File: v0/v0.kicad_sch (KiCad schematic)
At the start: 20 parts, among them CON1 SNES-CONN, U1 SN74LV165APWR, U2 SN74LV165APWR, U3 SN74LV165APWR

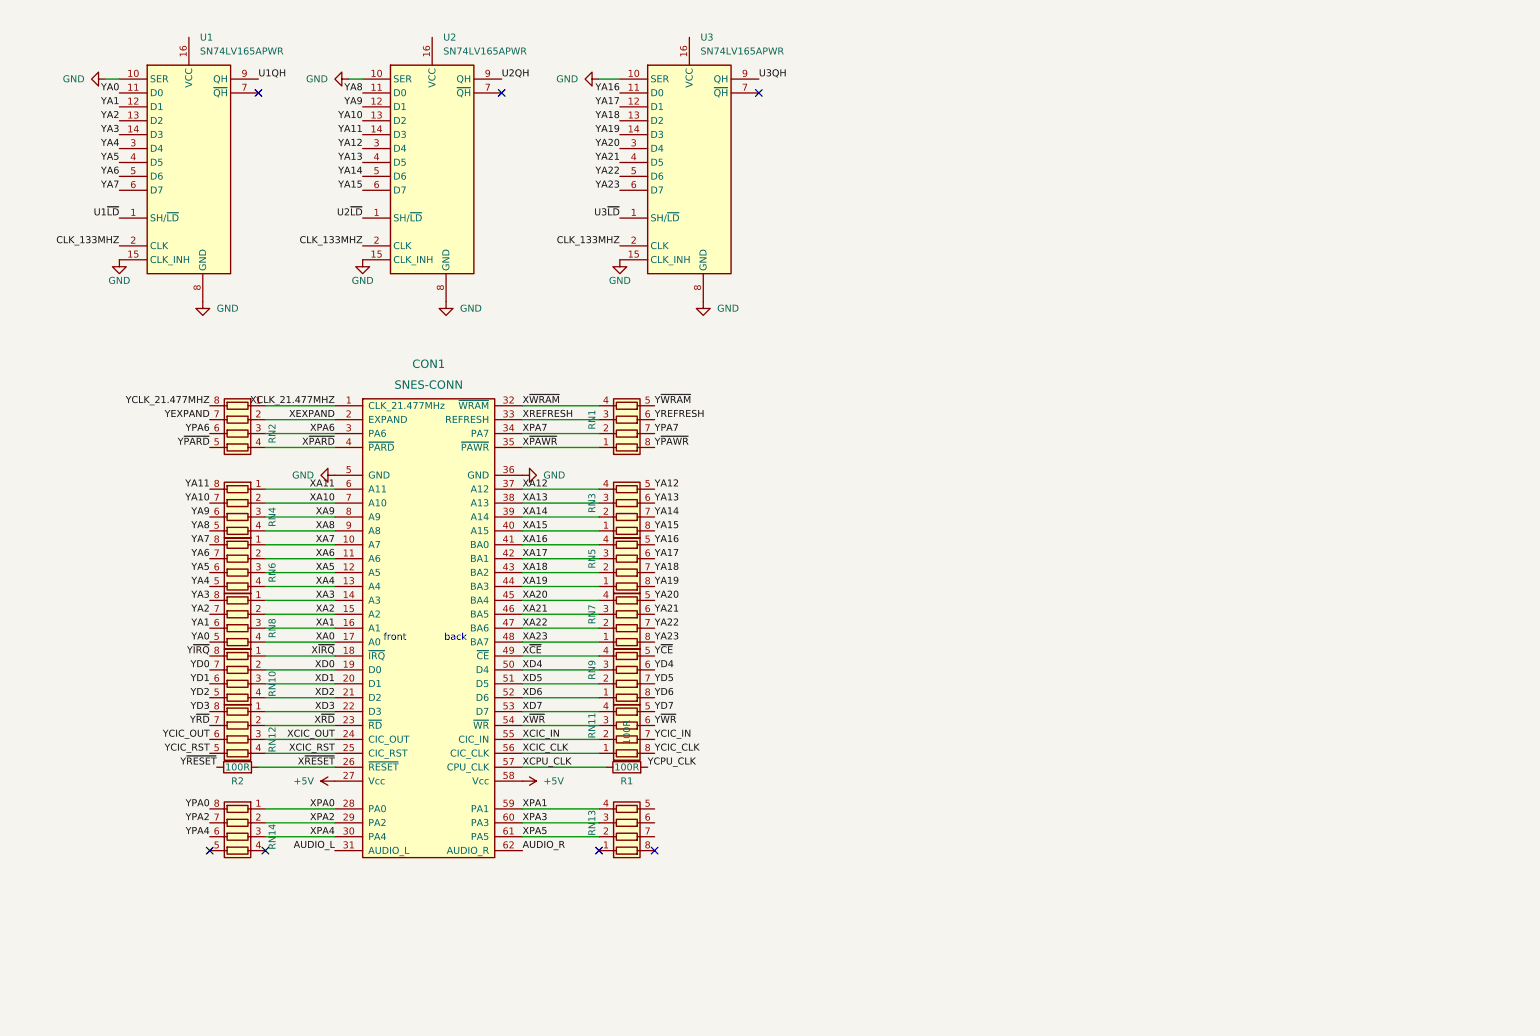
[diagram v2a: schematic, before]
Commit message: Added PIC12F and 3.3V supply; routed all nets
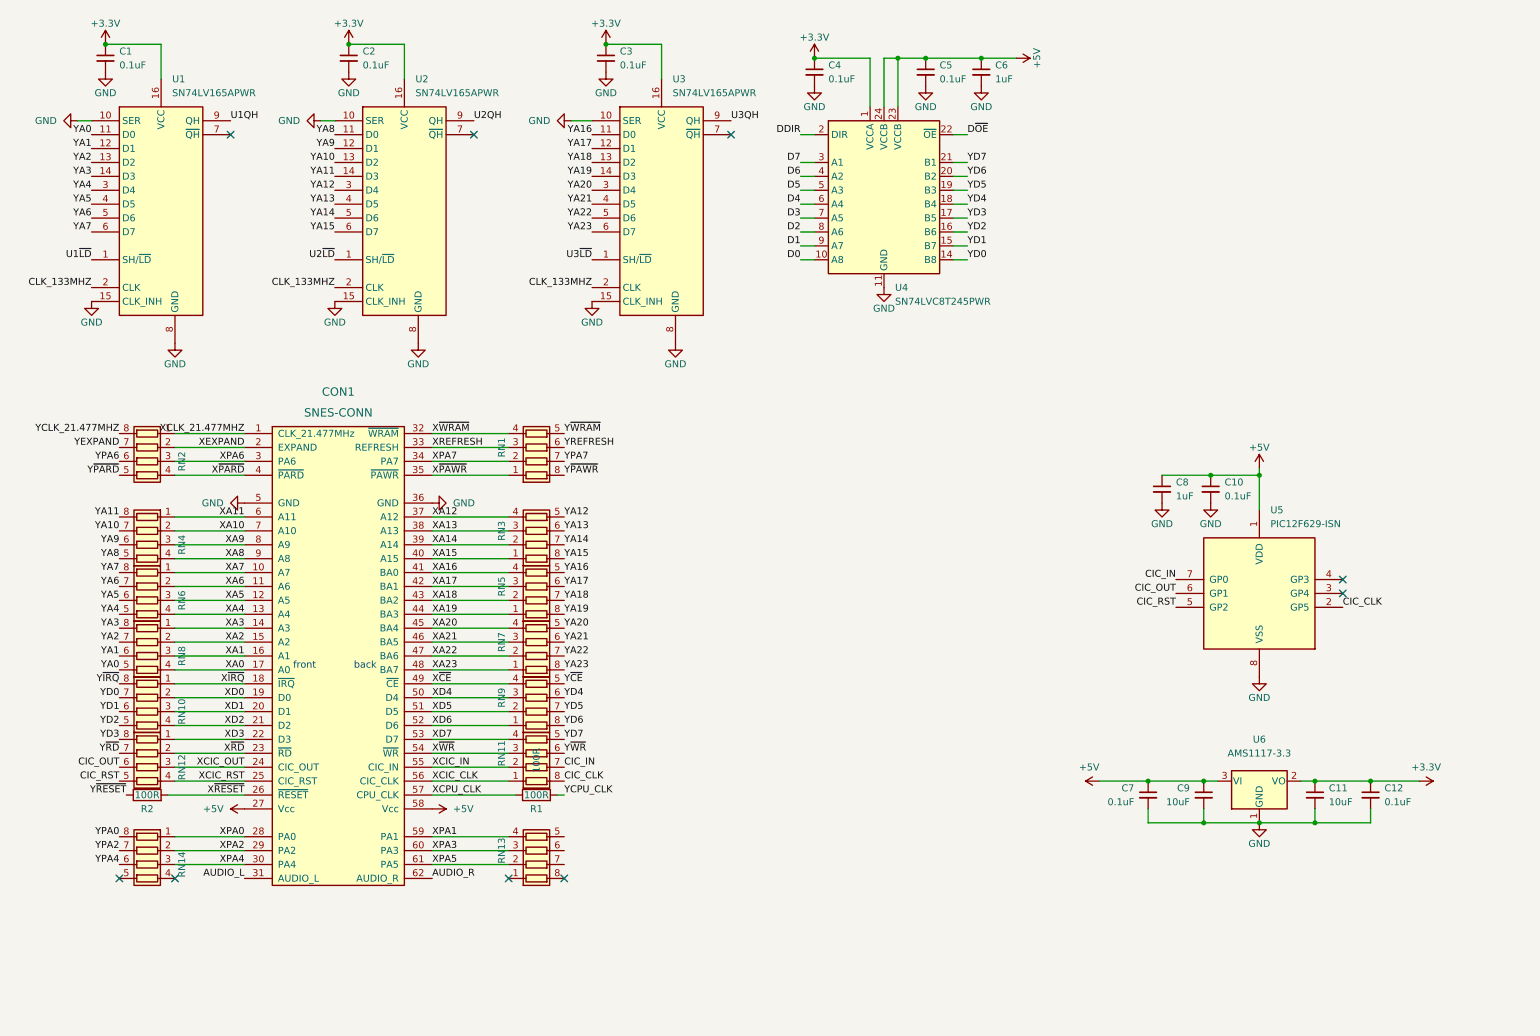
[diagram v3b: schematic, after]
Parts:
- added C1, C10, C12, C2, C3, C4, C5, C7: 0.1uF, Capacitor_SMD:C_1206_3216Metric_Pad1.33x1.80mm_HandSolder, symbol Device:C_Small
- added C11, C9: 10uF, Capacitor_SMD:C_1206_3216Metric_Pad1.33x1.80mm_HandSolder, symbol Device:C_Small
- added C6, C8: 1uF, Capacitor_SMD:C_1206_3216Metric_Pad1.33x1.80mm_HandSolder, symbol Device:C_Small
- added U4: SN74LVC8T245PWR, Package_SO:TSSOP-24_4.4x7.8mm_P0.65mm, symbol Logic_LevelTranslator:SN74AVC8T245PW
- added U5: PIC12F629-ISN, Package_SO:SOIC-8_3.9x4.9mm_P1.27mm, symbol MCU_Microchip_PIC12:PIC12F629-ISN
- added U6: AMS1117-3.3, Package_TO_SOT_SMD:SOT-223-3_TabPin2, symbol Regulator_Linear:AMS1117-3.3
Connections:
- net +5V: now also C10.1, C5.1, C6.1, C7.1, C8.1, C9.1, U4.23 (VCCB), U4.24 (VCCB), U5.1 (VDD), U6.3 (VI)
- net GND: now also C1.2, C10.2, C11.2, C12.2, C2.2, C3.2, C4.2, C5.2, C6.2, C7.2, C8.2, C9.2, U4.11 (GND), U4.12 (GND), U4.13 (GND), U5.8 (VSS), U6.1 (GND)
- net YD0: now also U4.14 (B8)
- net YD1: now also U4.15 (B7)
- net YD2: now also U4.16 (B6)
- net YD3: now also U4.17 (B5)
- net YD4: now also U4.18 (B4)
- net YD5: now also U4.19 (B3)
- net YD6: now also U4.20 (B2)
- net YD7: now also U4.21 (B1)
- net +3.3V: now reaches U3.16 (VCC)
- net +3.3V: now also U1.16 (VCC), U2.16 (VCC), C1.1, C11.1, C12.1, C2.1, C3.1, C4.1, U4.1 (VCCA), U6.2 (VO)
- net YCIC_CLK renamed CIC_CLK
- net CIC_CLK: now also U5.2 (GP5)
- net YCIC_IN renamed CIC_IN
- net CIC_IN: now also U5.7 (GP0)
- net YCIC_OUT renamed CIC_OUT
- net CIC_OUT: now also U5.6 (GP1)
- net YCIC_RST renamed CIC_RST
- net CIC_RST: now also U5.5 (GP2)
- new net D0: U4.10 (A8)
- new net D1: U4.9 (A7)
- new net D2: U4.8 (A6)
- new net D3: U4.7 (A5)
- new net D4: U4.6 (A4)
- new net D5: U4.5 (A3)
- new net D6: U4.4 (A2)
- new net D7: U4.3 (A1)
- new net DDIR: U4.2 (DIR)
- new net D~{OE}: U4.22 (~{OE})
- no-connect marks 7 -> 9
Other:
- moved on the sheet: CON1, R1, R2, RN1, RN10, RN11, RN12, RN13, RN14, RN2, RN3, RN4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

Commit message: Added RPi Pico footprint and routed traces to it
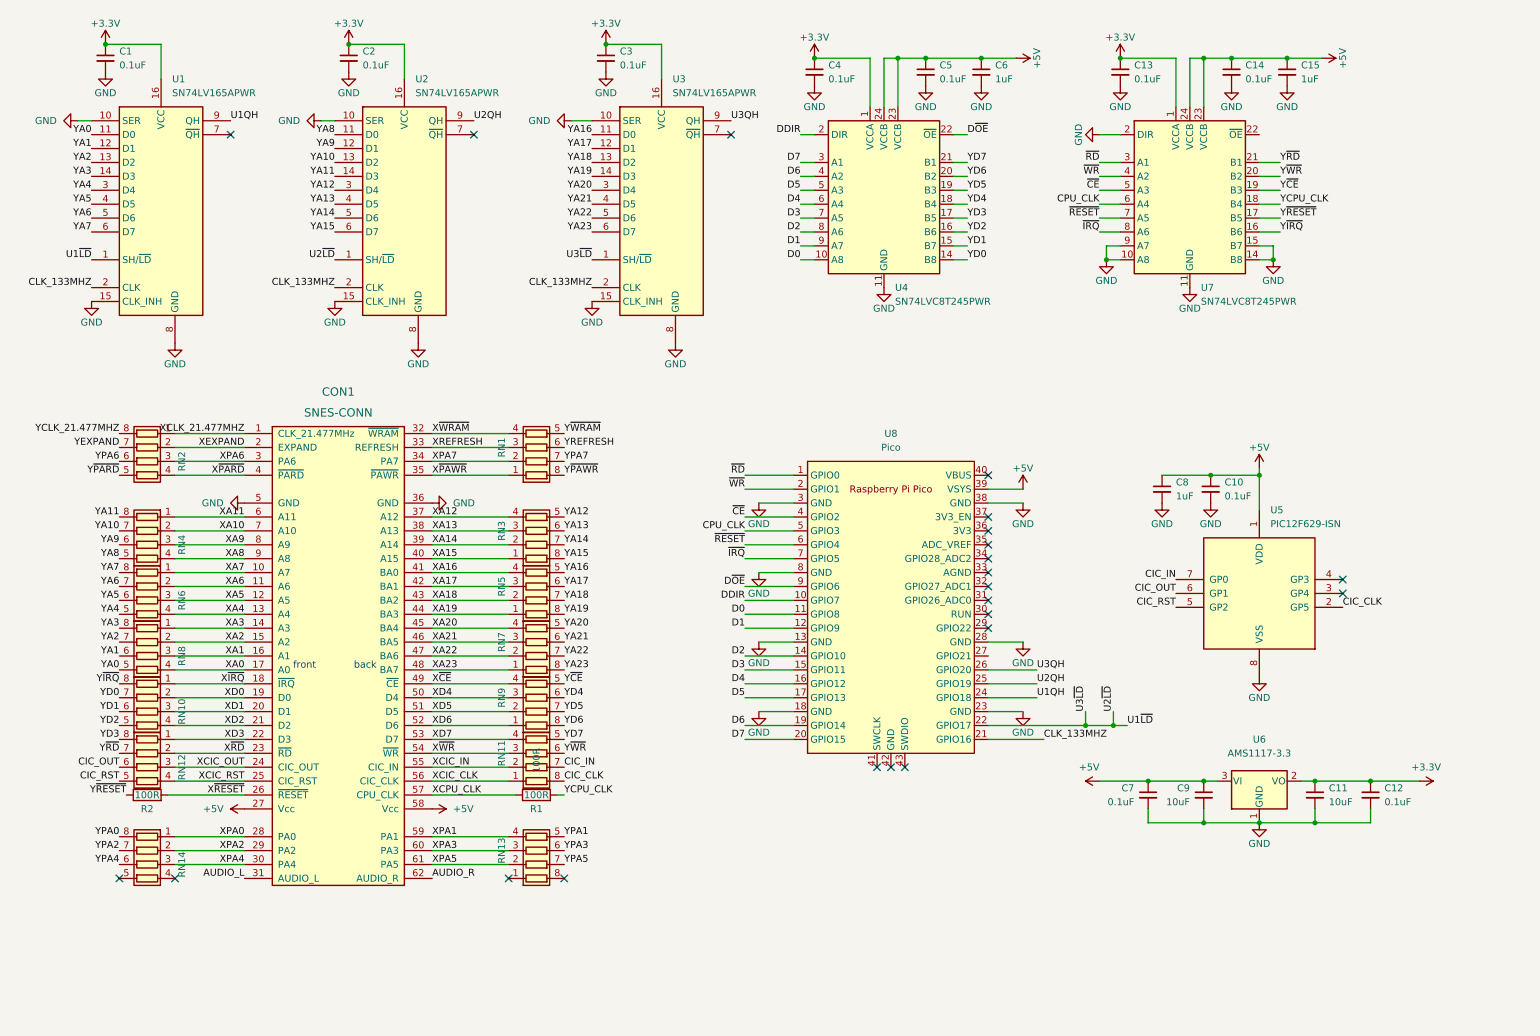
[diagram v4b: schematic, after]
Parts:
- added C13, C14: 0.1uF, Capacitor_SMD:C_1206_3216Metric_Pad1.33x1.80mm_HandSolder, symbol Device:C_Small
- added C15: 1uF, Capacitor_SMD:C_1206_3216Metric_Pad1.33x1.80mm_HandSolder, symbol Device:C_Small
- added U7: SN74LVC8T245PWR, Package_SO:TSSOP-24_4.4x7.8mm_P0.65mm, symbol Logic_LevelTranslator:SN74AVC8T245PW
- added U8: Pico, RP-Pico:RPi_Pico_SMD_TH, symbol MCU_RaspberryPi_and_Boards:Pico
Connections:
- net U2~{LD} is gone; now on net U1~{LD}: U2.1 (SH/~{LD})
- net U3~{LD} is gone; now on net U1~{LD}: U3.1 (SH/~{LD})
- net +3.3V: now also C13.1, U7.1 (VCCA)
- net +5V: now also C14.1, C15.1, U7.23 (VCCB), U7.24 (VCCB), U8.39 (VSYS)
- net CLK_133MHZ: now also U8.21 (GPIO16)
- net D0: now also U8.11 (GPIO8)
- net D1: now also U8.12 (GPIO9)
- net D2: now also U8.14 (GPIO10)
- net D3: now also U8.15 (GPIO11)
- net D4: now also U8.16 (GPIO12)
- net D5: now also U8.17 (GPIO13)
- net D6: now also U8.19 (GPIO14)
- net D7: now also U8.20 (GPIO15)
- net DDIR: now also U8.10 (GPIO7)
- net D~{OE}: now also U8.9 (GPIO6)
- net GND: now also C13.2, C14.2, C15.2, U7.10 (A8), U7.11 (GND), U7.12 (GND), U7.13 (GND), U7.14 (B8), U7.15 (B7), U7.2 (DIR), U7.9 (A7), U8.13 (GND), U8.18 (GND), U8.23 (GND), U8.28 (GND), U8.3 (GND), U8.38 (GND), U8.8 (GND)
- net U1QH: now also U8.24 (GPIO18)
- net U1~{LD}: now also U8.22 (GPIO17)
- net U2QH: now also U8.25 (GPIO19)
- net U3QH: now also U8.26 (GPIO20)
- net YCPU_CLK: now also U7.18 (B4)
- net Y~{CE}: now also U7.19 (B3)
- net Y~{IRQ}: now also U7.16 (B6)
- net Y~{RD}: now also U7.21 (B1)
- net Y~{RESET}: now also U7.17 (B5)
- net Y~{WR}: now also U7.20 (B2)
- net YPA1: now reaches RN13.5 (R4.2)
- net YPA3: now reaches RN13.6 (R3.2)
- net YPA5: now reaches RN13.7 (R2.2)
- new net CPU_CLK: U7.6 (A4), U8.5 (GPIO3)
- new net ~{CE}: U7.5 (A3), U8.4 (GPIO2)
- new net ~{IRQ}: U7.8 (A6), U8.7 (GPIO5)
- new net ~{RD}: U7.3 (A1), U8.1 (GPIO0)
- new net ~{RESET}: U7.7 (A5), U8.6 (GPIO4)
- new net ~{WR}: U7.4 (A2), U8.2 (GPIO1)
- no-connect marks 9 -> 22

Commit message: Connect /OE to GND; fix up minor routing
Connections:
- net GND: now also U7.22 (~{OE}); no longer U7.10 (A8), U7.14 (B8), U7.15 (B7), U7.9 (A7)
- new net U7A7: U7.9 (A7)
- new net U7A8: U7.10 (A8)
- new net U7B7: U7.15 (B7)
- new net U7B8: U7.14 (B8)
- no-connect marks 22 -> 27
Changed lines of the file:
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@@
   (junction (at 72.39 17.78) (diameter 0) (color 0 0 0 0)
   )
-  (junction (at 210.82 57.15) (diameter 0) (color 0 0 0 0)
-  )
   (junction (at 212.09 142.24) (diameter 0) (color 0 0 0 0)
   )
@@
   )
   (junction (at 213.36 20.32) (diameter 0) (color 0 0 0 0)
-  )
-  (junction (at 241.3 57.15) (diameter 0) (color 0 0 0 0)
   )
   (junction (at 238.76 160.02) (diameter 0) (color 0 0 0 0)
@@
   (no_connect (at 30.48 170.18))
   (no_connect (at 40.64 170.18))
+  (no_connect (at 213.36 54.61))
+  (no_connect (at 213.36 57.15))
   (no_connect (at 101.6 170.18))
   (no_connect (at 111.76 170.18))
+  (no_connect (at 189.23 129.54))
   (no_connect (at 189.23 111.76))
   (no_connect (at 189.23 109.22))
@@
   (no_connect (at 50.8 34.29))
   (no_connect (at 95.25 34.29))
+  (no_connect (at 238.76 54.61))
+  (no_connect (at 238.76 57.15))
   (no_connect (at 254 118.11))
   (no_connect (at 254 115.57))
@@
     (stroke (width 0) (type default) (color 0 0 0 0))
   )
-  (wire (pts (xy 241.3 57.15) (xy 238.76 57.15))
-    (stroke (width 0) (type default) (color 0 0 0 0))
-  )
   (wire (pts (xy 144.78 104.14) (xy 153.67 104.14))
     (stroke (width 0) (type default) (color 0 0 0 0))
@@
     (stroke (width 0) (type default) (color 0 0 0 0))
   )
-  (wire (pts (xy 210.82 57.15) (xy 213.36 57.15))
-    (stroke (width 0) (type default) (color 0 0 0 0))
-  )
   (wire (pts (xy 119.38 17.78) (xy 129.54 17.78))
     (stroke (width 0) (type default) (color 0 0 0 0))
@@
     (stroke (width 0) (type default) (color 0 0 0 0))
   )
-  (wire (pts (xy 241.3 54.61) (xy 241.3 57.15))
-    (stroke (width 0) (type default) (color 0 0 0 0))
-  )
   (wire (pts (xy 101.6 132.08) (xy 87.63 132.08))
     (stroke (width 0) (type default) (color 0 0 0 0))
@@
     (stroke (width 0) (type default) (color 0 0 0 0))
   )
-  (wire (pts (xy 210.82 54.61) (xy 210.82 57.15))
-    (stroke (width 0) (type default) (color 0 0 0 0))
-  )
   (wire (pts (xy 218.44 160.02) (xy 218.44 157.48))
     (stroke (width 0) (type default) (color 0 0 0 0))
@@
     (stroke (width 0) (type default) (color 0 0 0 0))
   )
-  (wire (pts (xy 238.76 54.61) (xy 241.3 54.61))
-    (stroke (width 0) (type default) (color 0 0 0 0))
-  )
   (wire (pts (xy 220.98 96.52) (xy 229.87 96.52))
     (stroke (width 0) (type default) (color 0 0 0 0))
@@
     (stroke (width 0) (type default) (color 0 0 0 0))
   )
+  (wire (pts (xy 242.57 34.29) (xy 238.76 34.29))
+    (stroke (width 0) (type default) (color 0 0 0 0))
+  )
   (wire (pts (xy 40.64 165.1) (xy 53.34 165.1))
     (stroke (width 0) (type default) (color 0 0 0 0))
   )
-  (wire (pts (xy 213.36 54.61) (xy 210.82 54.61))
-    (stroke (width 0) (type default) (color 0 0 0 0))
-  )
   (wire (pts (xy 101.6 91.44) (xy 87.63 91.44))
     (stroke (width 0) (type default) (color 0 0 0 0))
@@
     (effects (font (size 1.27 1.27)) (justify left bottom))
   )
+  (label "U7B7" (at 238.76 54.61 0)
+    (effects (font (size 1.27 1.27)) (justify left bottom))
+  )
   (label "XPA4" (at 53.34 167.64 180)
     (effects (font (size 1.27 1.27)) (justify right bottom))
@@
     (effects (font (size 1.27 1.27)) (justify left bottom))
   )
+  (label "U7B8" (at 238.76 57.15 0)
+    (effects (font (size 1.27 1.27)) (justify left bottom))
+  )
   (label "YD6" (at 185.42 41.91 0)
     (effects (font (size 1.27 1.27)) (justify left bottom))
@@
     (effects (font (size 1.27 1.27)) (justify right bottom))
   )
+  (label "U7A7" (at 213.36 54.61 180)
+    (effects (font (size 1.27 1.27)) (justify right bottom))
+  )
   (label "CPU_CLK" (at 144.78 106.68 180)
     (effects (font (size 1.27 1.27)) (justify right bottom))
@@
   )
   (label "~{RD}" (at 209.55 39.37 180)
+    (effects (font (size 1.27 1.27)) (justify right bottom))
+  )
+  (label "U7A8" (at 213.36 57.15 180)
     (effects (font (size 1.27 1.27)) (justify right bottom))
   )
@@
     (pin "1")
   )
-  (symbol (lib_id "power:GND") (at 210.82 57.15 0) (unit 1)
-    (in_bom yes) (on_board yes)
-    (property "Reference" "#PWR021" (id 0) (at 210.82 63.5 0)
-      (effects (font (size 1.27 1.27)) hide)
-    )
-    (property "Value" "GND" (id 1) (at 210.82 60.96 0))
-    (property "Footprint" "" (id 2) (at 210.82 57.15 0)
-      (effects (font (size 1.27 1.27)) hide)
-    )
-    (property "Datasheet" "" (id 3) (at 210.82 57.15 0)
-      (effects (font (size 1.27 1.27)) hide)
-    )
-    (pin "1")
-  )
   (symbol (lib_id "Device:R_Pack04") (at 35.56 129.54 90) (mirror x) (unit 1)
     (in_bom yes) (on_board yes)
@@
     (pin "1")
   )
+  (symbol (lib_id "power:GND") (at 242.57 34.29 90) (unit 1)
+    (in_bom yes) (on_board yes)
+    (property "Reference" "#PWR0122" (id 0) (at 248.92 34.29 0)
+      (effects (font (size 1.27 1.27)) hide)
+    )
+    (property "Value" "GND" (id 1) (at 246.38 34.29 0))
+    (property "Footprint" "" (id 2) (at 242.57 34.29 0)
+      (effects (font (size 1.27 1.27)) hide)
+    )
+    (property "Datasheet" "" (id 3) (at 242.57 34.29 0)
+      (effects (font (size 1.27 1.27)) hide)
+    )
+    (pin "1")
+  )
   (symbol (lib_id "Device:R") (at 35.56 154.94 90) (unit 1)
     (in_bom yes) (on_board yes)
@@
     (pin "1")
     (pin "2")
-  )
-  (symbol (lib_id "power:GND") (at 241.3 57.15 0) (unit 1)
-    (in_bom yes) (on_board yes)
-    (property "Reference" "#PWR026" (id 0) (at 241.3 63.5 0)
-      (effects (font (size 1.27 1.27)) hide)
-    )
-    (property "Value" "GND" (id 1) (at 241.3 60.96 0))
-    (property "Footprint" "" (id 2) (at 241.3 57.15 0)
-      (effects (font (size 1.27 1.27)) hide)
-    )
-    (property "Datasheet" "" (id 3) (at 241.3 57.15 0)
-      (effects (font (size 1.27 1.27)) hide)
-    )
-    (pin "1")
   )
   (symbol (lib_id "Device:C_Small") (at 243.84 22.86 0) (unit 1)
@@
       (reference "#PWR020") (unit 1) (value "GND") (footprint "")
     )
-    (path "/4dc1ec9c-b8a5-4826-965f-f2f57400547b"
-      (reference "#PWR021") (unit 1) (value "GND") (footprint "")
-    )
     (path "/1591e10b-25c7-4634-84f2-f42bed76aed5"
       (reference "#PWR022") (unit 1) (value "+3.3V") (footprint "")
@@
       (reference "#PWR025") (unit 1) (value "GND") (footprint "")
     )
-    (path "/e039e915-3b11-4211-ad1c-8433133dedd2"
-      (reference "#PWR026") (unit 1) (value "GND") (footprint "")
-    )
     (path "/ceeb9bdb-7eb9-42d6-9320-361ca242c5d5"
       (reference "#PWR027") (unit 1) (value "GND") (footprint "")
@@
       (reference "#PWR0121") (unit 1) (value "GND") (footprint "")
     )
+    (path "/d7fd33ba-6e25-4913-ba45-aedd445728d2"
+      (reference "#PWR0122") (unit 1) (value "GND") (footprint "")
+    )
     (path "/bbdbe439-63b1-44e9-b277-34f4e5557d1a"
